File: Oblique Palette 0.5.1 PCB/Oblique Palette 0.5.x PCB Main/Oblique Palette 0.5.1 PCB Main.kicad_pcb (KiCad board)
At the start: 2 copper layers, 235 x 110 mm, 301 parts, among them J11 Conn_01x03_Male_Pin, J13 Conn_01x03_Male_Pin, J14 Conn_01x03_Male_Pin, J16 Conn_01x03_Female_Pin, J17 AudioJack2_SwitchT, J19 Conn_01x03_Female_Pin, J2 Conn_01x03_Male_Pin, J20 AudioJack2_SwitchT, J22 Conn_01x03_Female_Pin, J23 AudioJack2_SwitchT, J25 Conn_01x03_Female_Pin, J26 AudioJack2_SwitchT, J28 Conn_01x03_Female_Pin, J29 AudioJack2_SwitchT, J31 Conn_01x03_Female_Pin, J32 AudioJack2_SwitchT, J34 Conn_01x03_Female_Pin, J35 AudioJack2_SwitchT, J37 Conn_01x03_Female_Pin, J38 AudioJack2_SwitchT, J4 Conn_01x03_Male_Pin, J40 Conn_01x03_Female_Pin, J42 AudioJack2_SwitchT, J44 Conn_01x03_Female_Pin, J46 AudioJack2_SwitchT, J48 Conn_01x03_Female_Pin, J5 Conn_01x03_Male_Pin, J50 AudioJack2_SwitchT, J52 Conn_01x03_Female_Pin, J54 AudioJack2_SwitchT, J56 Conn_01x03_Female_Pin, J58 AudioJack2_SwitchT, J60 Conn_01x03_Female_Pin, J62 AudioJack2_SwitchT, J64 Conn_01x03_Female_Pin, J66 AudioJack2_SwitchT, J68 Conn_01x03_Female_Pin, J7 Conn_01x03_Male_Pin, J70 AudioJack2_SwitchT, J9 Conn_01x03_Male_Pin, U1 CD4051B, U10 MCP6004, U11 MCP4725xxx-xCH, U12 MCP6004, U13 MCP4725xxx-xCH, U14 MCP6004, U15 MCP4725xxx-xCH, U16 MCP6004, U17 MCP4725xxx-xCH, U18 MCP6004, U19 MCP4725xxx-xCH, U2 Pico, U20 MCP6004, U21 MCP4725xxx-xCH, U22 MCP6004, U23 MCP4725xxx-xCH, U24 MCP6004, U25 MCP4725xxx-xCH, U26 MCP6004, U3 MCP6004, U4 MCP6004, U5 MCP6004, U6 MCP6004, U7 MCP6004, U8 MCP6004, U9 MCP6004

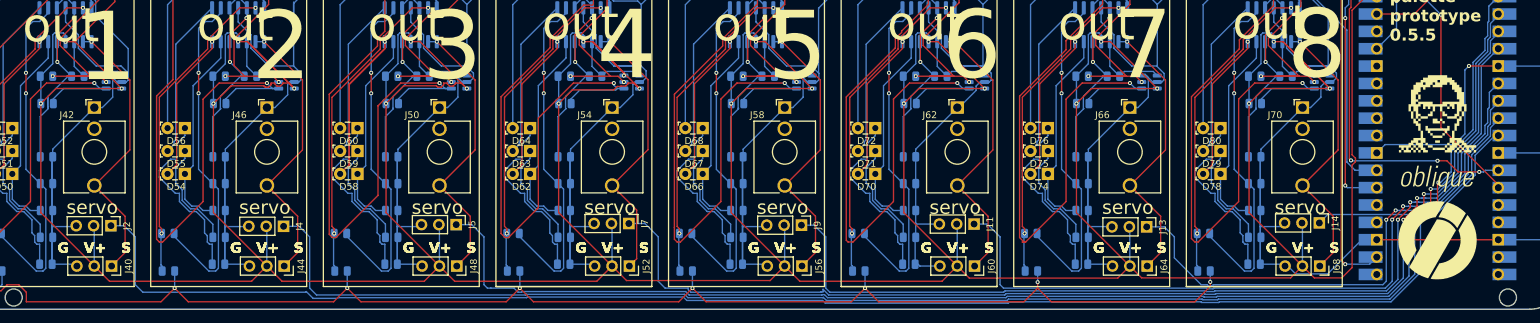
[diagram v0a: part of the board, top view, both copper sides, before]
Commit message: Corrected missing traces but good.
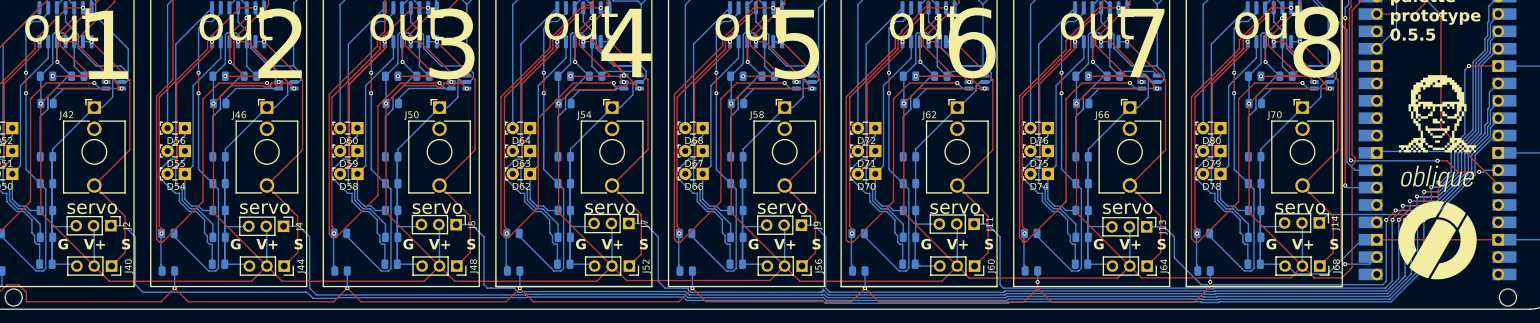
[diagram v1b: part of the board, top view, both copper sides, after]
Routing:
- net SERVO_4: track 164.3 -> 167.7 mm
- net SERVO_5: track 133.6 -> 135.6 mm
- net Net-(J52-Pin_1): track 40.4 -> 41.0 mm
- net VCC: vias 48 -> 49
